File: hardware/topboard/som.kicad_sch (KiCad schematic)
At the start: 17 parts, among them SW1 SW_DIP_x04, U1 CP3225-100.000-3.3-25-X-T-TR, U2 CP3225-125.000-3.3-25-X-T-TR, U3 AX3HAF1-135.0000T

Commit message: Assign most top-board footprints
Signed-off-by: gatecat <gatecat@ds0.me>
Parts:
- C1: footprint (none) -> Capacitor_SMD:C_0805_2012Metric
- C10, C5, C6, C7, C8, C9: footprint (none) -> Capacitor_SMD:C_0402_1005Metric
- C2, C3, C4: footprint (none) -> Capacitor_SMD:C_0603_1608Metric
- FB1: footprint (none) -> Inductor_SMD:L_0603_1608Metric
- R1: footprint (none) -> Resistor_SMD:R_0402_1005Metric
- SOM1: footprint (none) -> meowality:KRIA_K26
- SW1: footprint (none) -> Button_Switch_SMD:SW_DIP_SPSTx04_Slide_Copal_CHS-04B_W7.62mm_P1.27mm

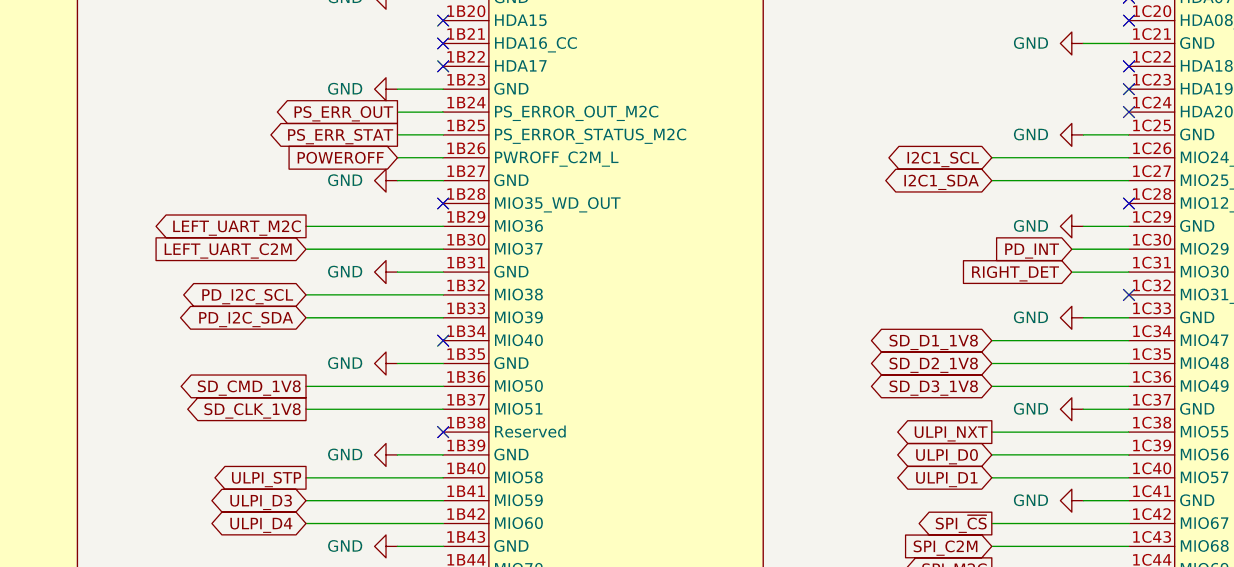
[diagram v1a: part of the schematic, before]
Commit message: Replace type-C power with good ol' barrel jack
Signed-off-by: gatecat <gatecat@ds0.me>
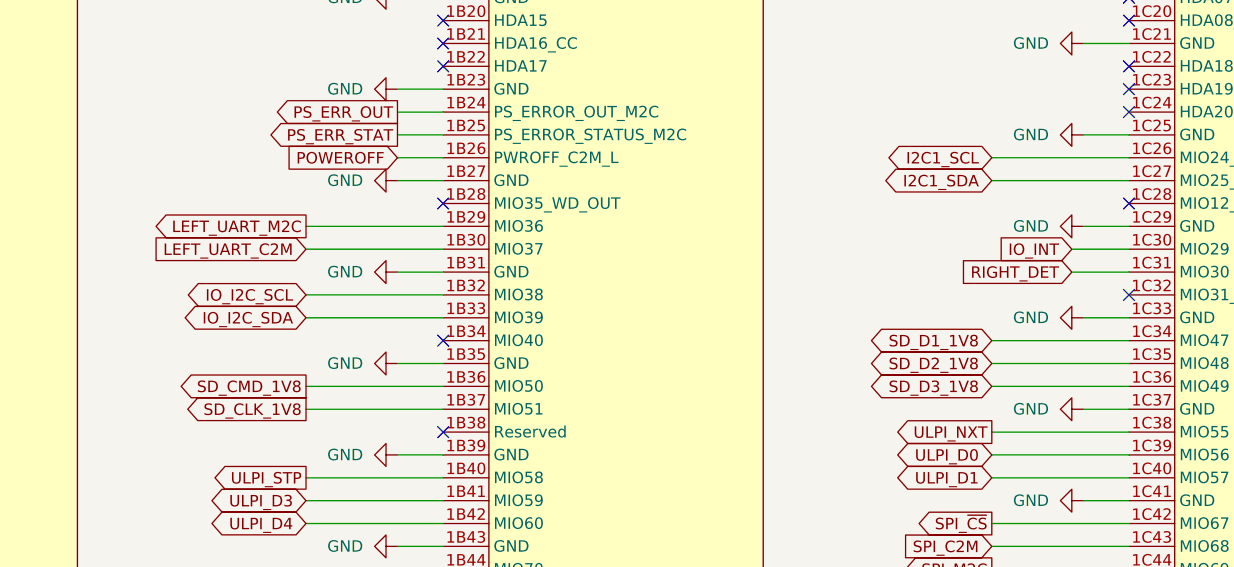
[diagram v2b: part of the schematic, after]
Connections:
- net PD_I2C_SCL renamed IO_I2C_SCL
- net PD_I2C_SDA renamed IO_I2C_SDA
- net PD_INT renamed IO_INT
